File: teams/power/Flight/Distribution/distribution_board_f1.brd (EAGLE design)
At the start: 90 x 90 mm, 278 parts, among them U2 TPS732XX, U3 TPS732XX

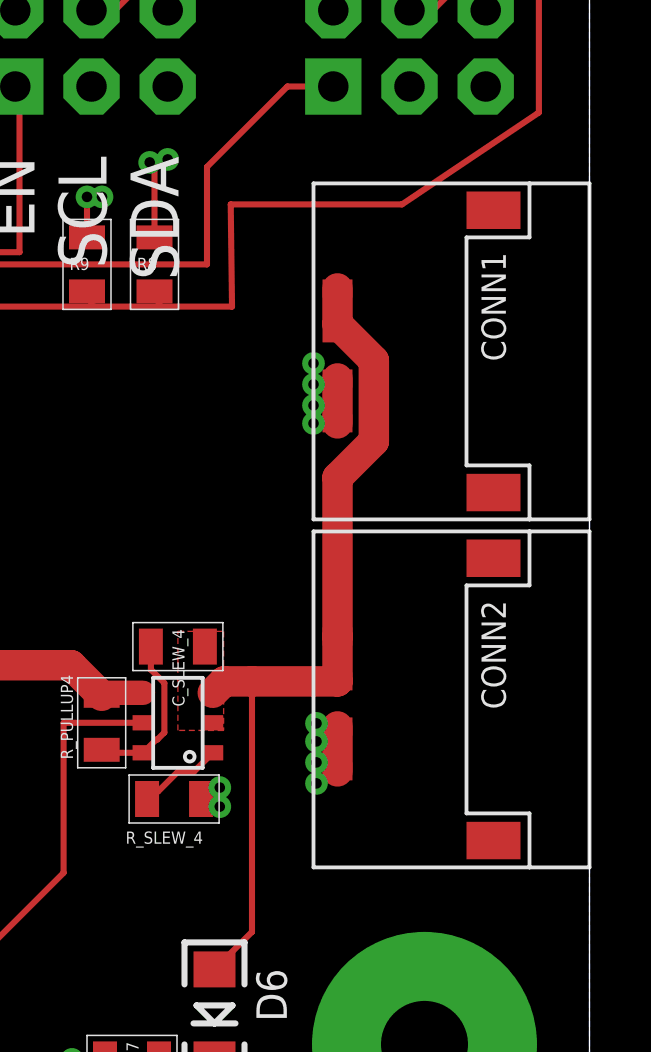
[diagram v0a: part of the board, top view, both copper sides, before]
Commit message: fixed distribution board. previous picolock library updating is broken. problem fixed by replacing with legacy part
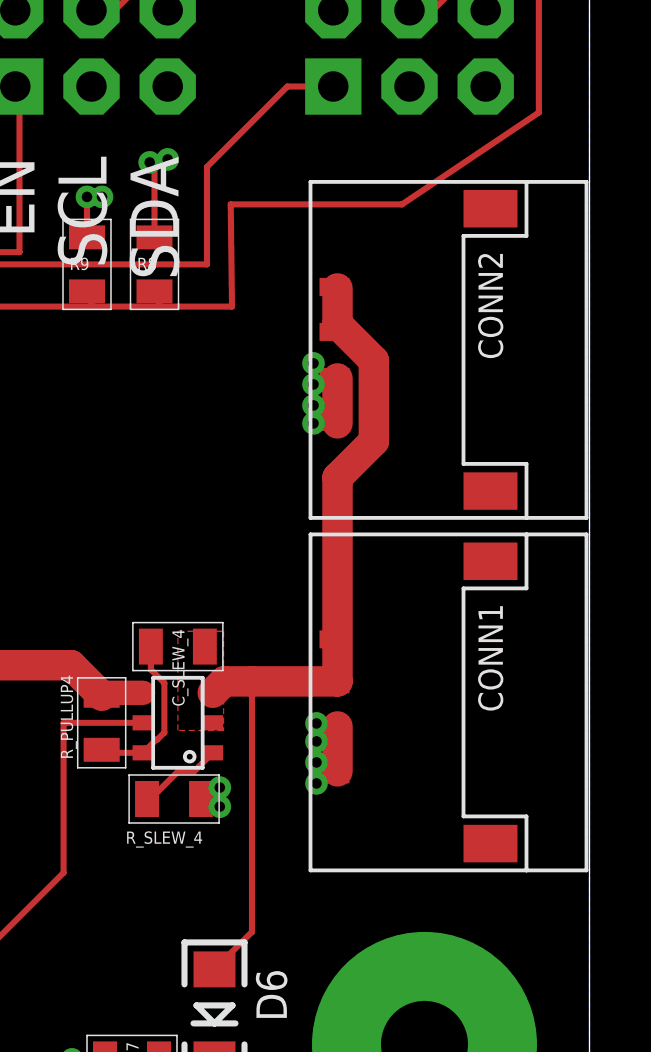
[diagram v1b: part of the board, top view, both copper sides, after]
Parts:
- CONN1, CONN2: value PICOLOCK_4PICOLOCK_4 -> PICOLOCK_4-LEGACY; device DubSat1 Components:PICOLOCK_4 -> DubSat1 Components:PICOLOCK_4-LEGACY
- moved CONN1 11.7 mm to (36.5, -26.0)
- moved CONN2 11.7 mm to (36.5, -14.2)
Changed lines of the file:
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@@
 <settings>
 <setting alwaysvectorfont="no"/>
+<setting keepoldvectorfont="yes"/>
 <setting verticaltext="up"/>
 </settings>
@@
 <element name="JP6" library="SparkFun-Connectors" package="2X3-NS" value="" x="28.4" y="-6.3"/>
 <element name="JP7" library="SparkFun-Connectors" package="2X3-NS" value="" x="-39.3" y="-13.3"/>
-<element name="CONN1" library="DubSat1 Components" package="PICOLOCK_4" package3d_urn="urn:adsk.eagle:package:2229882/2" value="PICOLOCK_4PICOLOCK_4" x="36.6" y="-14.3" rot="R270"/>
-<element name="CONN2" library="DubSat1 Components" package="PICOLOCK_4" package3d_urn="urn:adsk.eagle:package:2229882/2" value="PICOLOCK_4PICOLOCK_4" x="36.6" y="-25.9" rot="R270"/>
 <element name="C_SLEW_2" library="DubSat1 Components" package="0805" value=".1u" x="12.99" y="-18.22" rot="R270"/>
 <element name="R_PULLUP2" library="DubSat1 Components" package="0805" value="100k" x="15.53" y="-20.76" smashed="yes" rot="R180">
@@
 <element name="R44" library="DubSat1 Components" package="0805" value="5000" x="37.5" y="32.5"/>
 <element name="R45" library="DubSat1 Components" package="0805" value="5000" x="-42.5" y="23.5" rot="R270"/>
+<element name="CONN1" library="DubSat1 Components" package="PICOLOCK_4-LEGACY" value="PICOLOCK_4-LEGACY" x="36.5" y="-26" rot="R270"/>
+<element name="CONN2" library="DubSat1 Components" package="PICOLOCK_4-LEGACY" value="PICOLOCK_4-LEGACY" x="36.5" y="-14.25" rot="R270"/>
 </elements>
 <signals>
@@
 <via x="32.677" y="-31.574" extent="1-16" drill="0.35"/>
 <via x="32.677" y="-30.939" extent="1-16" drill="0.35"/>
-<contactref element="CONN1" pad="P$4"/>
-<contactref element="CONN1" pad="P$3"/>
-<contactref element="CONN2" pad="P$4"/>
-<contactref element="CONN2" pad="P$3"/>
 <wire x1="36.6" y1="-30.4" x2="36.6" y2="-28.9" width="1.016" layer="1"/>
 <wire x1="36.6" y1="-17.3" x2="36.6" y2="-18.8" width="1.016" layer="1"/>
@@
 <wire x1="-43" y1="39" x2="-36.5" y2="39" width="4" layer="16"/>
 <wire x1="-39.5" y1="35.25" x2="-39.5" y2="43.25" width="4" layer="16"/>
+<contactref element="CONN1" pad="P$3"/>
+<contactref element="CONN1" pad="P$4"/>
+<contactref element="CONN2" pad="P$3"/>
+<contactref element="CONN2" pad="P$4"/>
 <wire x1="33.4" y1="29.7" x2="33.1" y2="28.5" width="0" layer="19" extent="1-1"/>
 <wire x1="-35.19" y1="-7.204" x2="-35.19" y2="-7.32" width="0" layer="19" extent="1-1"/>
 <wire x1="29.31" y1="-0.204" x2="29.31" y2="-0.32" width="0" layer="19" extent="1-1"/>
+<wire x1="36.5" y1="-17.25" x2="36.6" y2="-17.3" width="0" layer="19" extent="1-1"/>
+<wire x1="36.5" y1="-18.75" x2="36.6" y2="-18.8" width="0" layer="19" extent="1-1"/>
 <wire x1="39.677" y1="3.768" x2="39.377" y2="3.452" width="0" layer="19" extent="1-1"/>
 <wire x1="-24.423" y1="3.768" x2="-24.723" y2="3.452" width="0" layer="19" extent="1-1"/>
@@
 <wire x1="-35.19" y1="-7.944" x2="-35.19" y2="-7.32" width="0" layer="19" extent="1-1"/>
 <wire x1="29.31" y1="-0.944" x2="29.31" y2="-0.32" width="0" layer="19" extent="1-1"/>
-<wire x1="36.6" y1="-28.9" x2="35.9" y2="-28.8" width="0" layer="19" extent="1-1"/>
+<wire x1="36.5" y1="-29" x2="35.9" y2="-28.8" width="0" layer="19" extent="1-1"/>
+<wire x1="36.6" y1="-28.9" x2="36.5" y2="-29" width="0" layer="19" extent="1-1"/>
+<wire x1="36.5" y1="-30.5" x2="36.6" y2="-30.4" width="0" layer="19" extent="1-1"/>
 <wire x1="32.4" y1="26" x2="33.15" y2="25.65" width="0" layer="19" extent="1-1"/>
 <wire x1="-32.1" y1="19" x2="-31.35" y2="18.65" width="0" layer="19" extent="1-1"/>
@@
 <vertex x="32.804" y="-29.034"/>
 </polygon>
-<contactref element="CONN1" pad="P$1"/>
-<contactref element="CONN1" pad="P$2"/>
-<contactref element="CONN2" pad="P$1"/>
-<contactref element="CONN2" pad="P$2"/>
 <wire x1="32.442" y1="-27.78" x2="32.822" y2="-27.4" width="1.016" layer="1"/>
 <wire x1="32.822" y1="-27.4" x2="33.75" y2="-27.4" width="1.016" layer="1"/>
 <wire x1="33.75" y1="-27.4" x2="36.6" y2="-27.4" width="1.016" layer="1"/>
-<wire x1="36.6" y1="-27.4" x2="36.6" y2="-25.9" width="1.016" layer="1"/>
-<wire x1="36.6" y1="-25.9" x2="36.6" y2="-20.6057875" width="1.016" layer="1"/>
+<wire x1="36.6" y1="-27.4" x2="36.6" y2="-20.6057875" width="1.016" layer="1"/>
 <wire x1="36.6" y1="-15.4942125" x2="36.6" y2="-14.3" width="1.016" layer="1"/>
 <wire x1="36.6" y1="-20.6057875" x2="37.8112" y2="-19.3945875" width="1.016" layer="1"/>
@@
 <wire x1="33.75" y1="-27.4" x2="33.75" y2="-35.75" width="0.2032" layer="1"/>
 <wire x1="33.75" y1="-35.75" x2="32.5" y2="-37" width="0.2032" layer="1"/>
-<wire x1="36.6" y1="-15.4942125" x2="36.6" y2="-15.8" width="0" layer="19" extent="1-1"/>
+<contactref element="CONN1" pad="P$1"/>
+<contactref element="CONN1" pad="P$2"/>
+<contactref element="CONN2" pad="P$1"/>
+<contactref element="CONN2" pad="P$2"/>
+<wire x1="36.6" y1="-14.3" x2="36.5" y2="-14.25" width="0" layer="19" extent="1-1"/>
+<wire x1="36.5" y1="-27.5" x2="36.6" y2="-27.4" width="0" layer="19" extent="1-1"/>
+<wire x1="36.5" y1="-15.75" x2="36.6" y2="-15.4942125" width="0" layer="19" extent="1-1"/>
+<wire x1="36.5" y1="-26" x2="36.6" y2="-27.4" width="0" layer="19" extent="1-1"/>
 </signal>
 <signal name="CANH">
@@
 which will not be processed correctly with this version.
 </note>
-<note version="8.3" severity="warning">
-Since Version 8.3, EAGLE supports URNs for individual library
-assets (packages, symbols, and devices). The URNs of those assets
-will not be understood (or retained) with this version.
-</note>
-<note version="8.3" severity="warning">
-Since Version 8.3, EAGLE supports the association of 3D packages
-with devices in libraries, schematics, and board files. Those 3D
-packages will not be understood (or retained) with this version.
-</note>
 </compatibility>

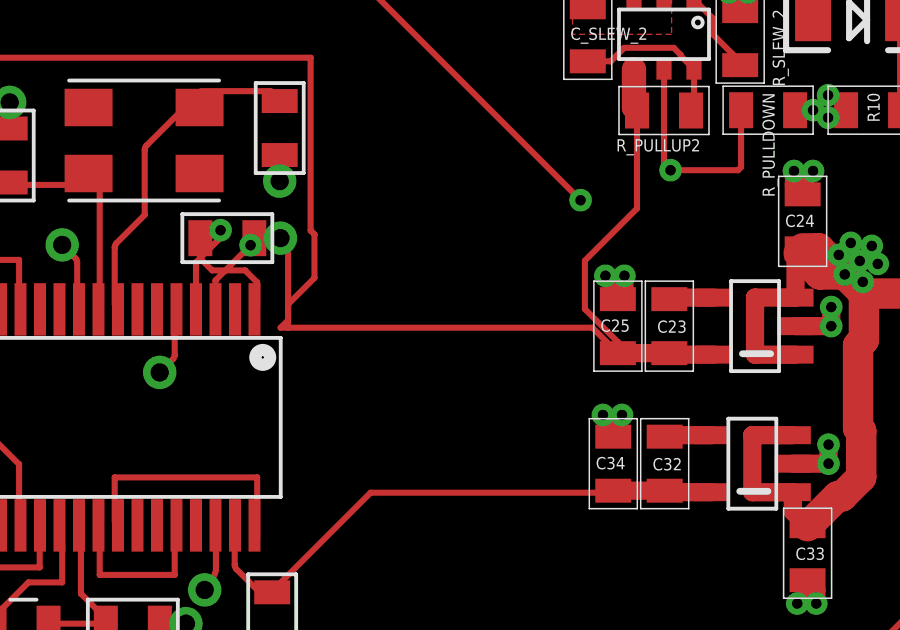
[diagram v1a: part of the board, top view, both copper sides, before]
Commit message: added ressetable fuse for MSP430 and remade GERBERs
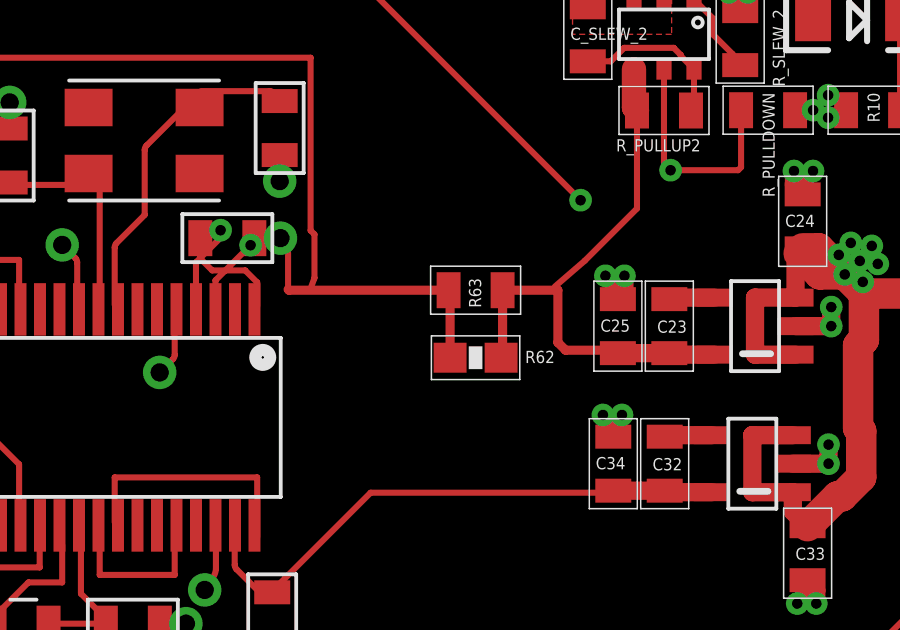
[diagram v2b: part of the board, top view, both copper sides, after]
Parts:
- added R62: (no value), DubSat1 Components:0603
- added R63: (no value), DubSat1 Components:0805
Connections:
- net 3.3V: now also R62.1, R62.2, R63.1, R63.2
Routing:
- net 3.3V: track 371.1 -> 375.8 mm
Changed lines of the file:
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@@
 <?xml version="1.0" encoding="utf-8"?>
 <!DOCTYPE eagle SYSTEM "eagle.dtd">
-<eagle version="8.7.1">
+<eagle version="8.4.2">
 <drawing>
 <settings>
@@
 <param name="checkRestrict" value="1"/>
 <param name="checkStop" value="0"/>
-<param name="checkValues" value="0"/>
 <param name="useDiameter" value="13"/>
 <param name="maxErrors" value="50"/>
@@
 <element name="CONN1" library="DubSat1 Components" package="PICOLOCK_4-LEGACY" value="PICOLOCK_4-LEGACY" x="36.5" y="-26" rot="R270"/>
 <element name="CONN2" library="DubSat1 Components" package="PICOLOCK_4-LEGACY" value="PICOLOCK_4-LEGACY" x="36.5" y="-14.25" rot="R270"/>
+<element name="R62" library="DubSat1 Components" package="0603" value="" x="9.25" y="-29"/>
+<element name="R63" library="DubSat1 Components" package="0805" value="" x="9.25" y="-26.75"/>
 </elements>
 <signals>
@@
 <wire x1="14.63" y1="-24.02811875" x2="14.63" y2="-20.76" width="0.2032" layer="1"/>
 <wire x1="12.89311875" y1="-25.765" x2="14.63" y2="-24.02811875" width="0.2032" layer="1"/>
-<wire x1="13.993" y1="-28.8475" x2="13.993" y2="-28.47855" width="0.2032" layer="1"/>
-<wire x1="13.993" y1="-28.47855" x2="12.89311875" y2="-27.37866875" width="0.2032" layer="1"/>
-<wire x1="12.89311875" y1="-27.37866875" x2="12.89311875" y2="-25.765" width="0.2032" layer="1"/>
+<wire x1="11.89311875" y1="-26.62866875" x2="12.89311875" y2="-25.765" width="0.2032" layer="1"/>
 <contactref element="BLK1" pad="3.3V@CAN2"/>
 <contactref element="BLK1" pad="3.3V_ANALOG@MSP2"/>
@@
 <contactref element="BLK1" pad="3.3V@MSP2"/>
 <contactref element="BLK1" pad="3.3V@CAN1"/>
-<wire x1="13.993" y1="-28.8475" x2="13.1455" y2="-28" width="0.2032" layer="1"/>
-<wire x1="3" y1="-28" x2="13.1455" y2="-28" width="0.2032" layer="1"/>
-<wire x1="3" y1="-28" x2="2.75" y2="-28" width="0.2032" layer="1"/>
 <wire x1="-15.4" y1="-38.85" x2="-15.8552" y2="-38.3948" width="0.2032" layer="1"/>
 <wire x1="-17.33125" y1="-24.8102" x2="-17.5098" y2="-24.98875" width="0.2032" layer="1"/>
@@
 <wire x1="-16.6864" y1="-24.1864" x2="-16.25" y2="-23.75" width="0.2032" layer="1"/>
 <wire x1="-16.25" y1="-23.75" x2="-16.25" y2="-23" width="0.2032" layer="1"/>
-<wire x1="3" y1="-27.75" x2="2.75" y2="-28" width="0.2032" layer="1"/>
-<wire x1="3" y1="-27.75" x2="3" y2="-25.5" width="0.2032" layer="1"/>
+<wire x1="3" y1="-26.72105" x2="3" y2="-25.5" width="0.2032" layer="1"/>
 <wire x1="-15.4" y1="-38.85" x2="-3.9" y2="-38.85" width="0.2032" layer="1"/>
 <wire x1="-3.9" y1="-38.85" x2="-3.75" y2="-38.7" width="0.2032" layer="1"/>
@@
 <wire x1="-15.89105" y1="-19" x2="3.75" y2="-19" width="0.2032" layer="1"/>
 <wire x1="3.8798" y1="-24.88875" x2="3.8798" y2="-26.34125" width="0.2032" layer="1"/>
-<wire x1="3" y1="-27.22105" x2="3" y2="-28" width="0.2032" layer="1"/>
-<wire x1="3.8798" y1="-26.34125" x2="3" y2="-27.22105" width="0.2032" layer="1"/>
+<wire x1="3" y1="-26.72105" x2="3" y2="-26.75" width="0.2032" layer="1"/>
+<wire x1="3.8798" y1="-26.34125" x2="3.735525" y2="-26.735525" width="0.2032" layer="1"/>
+<wire x1="3.735525" y1="-26.735525" x2="3.00056875" y2="-26.7210625" width="0.2032" layer="1"/>
+<wire x1="3.00056875" y1="-26.7210625" x2="3" y2="-26.72105" width="0.2032" layer="1"/>
 <wire x1="3.75" y1="-19" x2="3.75" y2="-24.75895" width="0.2032" layer="1"/>
 <wire x1="3.75" y1="-24.75895" x2="3.8798" y2="-24.88875" width="0.2032" layer="1"/>
@@
 <wire x1="15.5" y1="-16.25" x2="15.53" y2="-16.28" width="0.2032" layer="1"/>
 <wire x1="15.53" y1="-16.28" x2="15.53" y2="-17.058" width="0.2032" layer="1"/>
+<contactref element="R63" pad="2"/>
+<contactref element="R63" pad="1"/>
+<contactref element="R62" pad="1"/>
+<contactref element="R62" pad="2"/>
+<wire x1="8.35" y1="-26.75" x2="3.5" y2="-26.75" width="0.2032" layer="1"/>
+<wire x1="3.5" y1="-26.75" x2="3.735525" y2="-26.735525" width="0.2032" layer="1"/>
+<wire x1="8.35" y1="-26.75" x2="3.02950625" y2="-26.75" width="0.3048" layer="1"/>
+<wire x1="3.02950625" y1="-26.75" x2="3.00056875" y2="-26.7210625" width="0.3048" layer="1"/>
+<wire x1="8.4" y1="-29" x2="8.4" y2="-26.8" width="0.3048" layer="1"/>
+<wire x1="8.4" y1="-26.8" x2="8.35" y2="-26.75" width="0.3048" layer="1"/>
+<wire x1="10.15" y1="-26.75" x2="10.15" y2="-28.95" width="0.3048" layer="1"/>
+<wire x1="10.15" y1="-28.95" x2="10.1" y2="-29" width="0.3048" layer="1"/>
+<wire x1="11.993" y1="-26.75" x2="10.15" y2="-26.75" width="0.3048" layer="1"/>
+<wire x1="13.993" y1="-28.8475" x2="13.8955" y2="-28.75" width="0.3048" layer="1"/>
+<wire x1="13.8955" y1="-28.75" x2="12.25" y2="-28.75" width="0.3048" layer="1"/>
+<wire x1="12.25" y1="-28.75" x2="11.993" y2="-28.493" width="0.3048" layer="1"/>
+<wire x1="11.993" y1="-28.493" x2="11.993" y2="-26.75" width="0.3048" layer="1"/>
 <wire x1="-16.6864" y1="-38.18465" x2="-16.1456" y2="-37.4912" width="0" layer="19" extent="1-1"/>
 <wire x1="-16.1258" y1="-20.5076" x2="-16.6864" y2="-19.79535" width="0" layer="19" extent="1-1"/>
 <wire x1="-3.155" y1="-37.865" x2="-3.75" y2="-38.7" width="0" layer="19" extent="1-1"/>
+<wire x1="10.1" y1="-29" x2="8.4" y2="-29" width="0" layer="19" extent="1-1"/>
+<wire x1="11.89311875" y1="-26.62866875" x2="11.993" y2="-26.75" width="0" layer="19" extent="1-1"/>
 <wire x1="14.53" y1="-17.058" x2="14.53" y2="-19.382" width="0" layer="19" extent="1-1"/>
 <wire x1="-32.3802" y1="-6.2992" x2="-32.3444875" y2="-6.2857125" width="0" layer="19" extent="1-1"/>
@@
 which will not be processed correctly with this version.
 </note>
+<note version="8.3" severity="warning">
+Since Version 8.3, EAGLE supports URNs for individual library
+assets (packages, symbols, and devices). The URNs of those assets
+will not be understood (or retained) with this version.
+</note>
 </compatibility>
